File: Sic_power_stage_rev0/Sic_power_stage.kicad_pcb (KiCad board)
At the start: 4 copper layers, 242.5 x 94.5 mm, 153 parts, among them J1 20021321-00006C4LF, J2 20021321-00006C4LF, J3 20021321-00006C4LF, J4 20021321-00006C4LF, J5 20021321-00006C4LF, J6 20021321-00006C4LF, J7 20021321-00006C4LF, J8 20021321-00006C4LF, Q1 NTBG014N120M3P, Q10 NTBG014N120M3P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

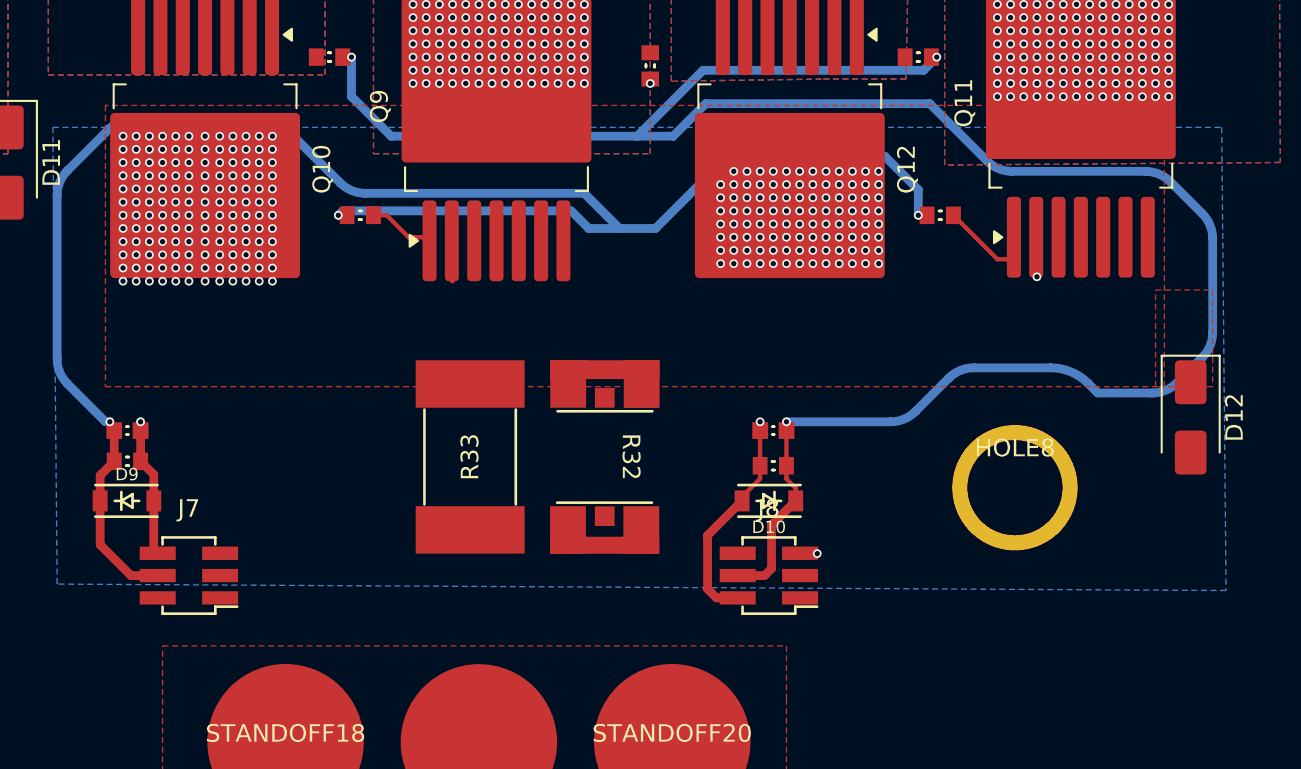
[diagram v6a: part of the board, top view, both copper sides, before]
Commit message: Sic: Define route for SHUNT leg C
Signed-off-by: Ayarde Christian <christianayarde@gmail.com>
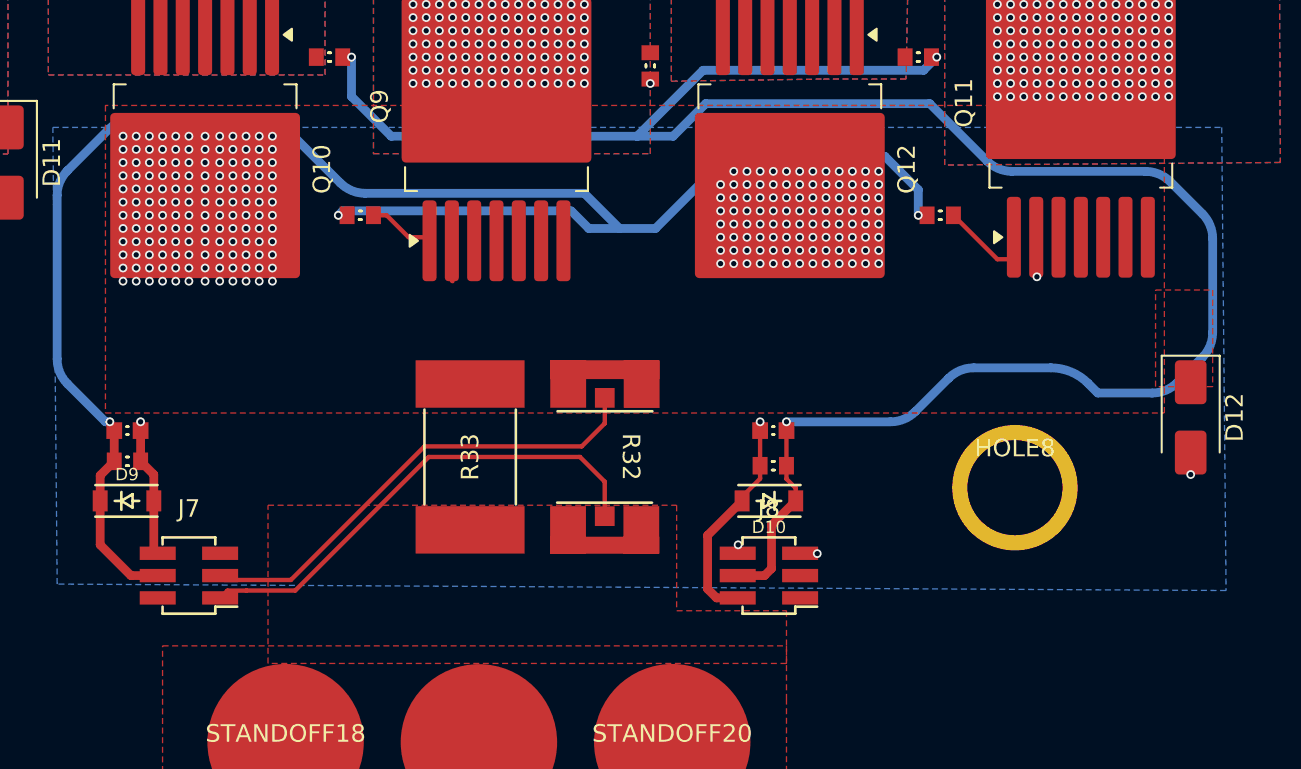
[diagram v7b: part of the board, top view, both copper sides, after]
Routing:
- net /Half Bridge C/D_BOT: track 0.00 -> 32.1 mm, vias 0 -> 2
- net /Half Bridge C/SHUNT-: track 0.00 -> 27.8 mm
- net /Half Bridge C/SHUNT+: track 0.00 -> 27.1 mm
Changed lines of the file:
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@@
 	)
 	(segment
+		(start 55.776 24.356)
+		(end 55.776 24.351)
+		(width 0.25)
+		(layer "F.Cu")
+		(net 22)
+	)
+	(segment
+		(start 76.16 18.16)
+		(end 76.16 20.12)
+		(width 0.25)
+		(layer "F.Cu")
+		(net 22)
+	)
+	(segment
+		(start 55.776 24.351)
+		(end 58.549058 24.351)
+		(width 0.25)
+		(layer "F.Cu")
+		(net 22)
+	)
+	(segment
+		(start 66.150058 16.75)
+		(end 74.75 16.75)
+		(width 0.25)
+		(layer "F.Cu")
+		(net 22)
+	)
+	(segment
+		(start 58.549058 24.351)
+		(end 66.150058 16.75)
+		(width 0.25)
+		(layer "F.Cu")
+		(net 22)
+	)
+	(segment
+		(start 54.275 24.77)
+		(end 54.689 24.356)
+		(width 0.25)
+		(layer "F.Cu")
+		(net 22)
+	)
+	(segment
+		(start 74.75 16.75)
+		(end 76.16 18.16)
+		(width 0.25)
+		(layer "F.Cu")
+		(net 22)
+	)
+	(segment
+		(start 54.689 24.356)
+		(end 55.776 24.356)
+		(width 0.25)
+		(layer "F.Cu")
+		(net 22)
+	)
+	(segment
+		(start 65.901116 16.149)
+		(end 58.300116 23.75)
+		(width 0.25)
+		(layer "F.Cu")
+		(net 23)
+	)
+	(segment
+		(start 76.1615 14.8385)
+		(end 74.851 16.149)
+		(width 0.25)
+		(layer "F.Cu")
+		(net 23)
+	)
+	(segment
+		(start 76.1615 13.389)
+		(end 76.1615 14.8385)
+		(width 0.25)
+		(layer "F.Cu")
+		(net 23)
+	)
+	(segment
+		(start 58.300116 23.75)
+		(end 54.525 23.75)
+		(width 0.25)
+		(layer "F.Cu")
+		(net 23)
+	)
+	(segment
+		(start 54.525 23.75)
+		(end 54.275 23.5)
+		(width 0.25)
+		(layer "F.Cu")
+		(net 23)
+	)
+	(segment
+		(start 74.851 16.149)
+		(end 65.901116 16.149)
+		(width 0.25)
+		(layer "F.Cu")
+		(net 23)
+	)
+	(segment
 		(start 78.75 -4.75)
 		(end 78.75 -4.5)
@@
 	)
 	(segment
+		(start 83.725 21.775)
+		(end 83.75 21.75)
+		(width 0.25)
+		(layer "F.Cu")
+		(net 26)
+	)
+	(segment
+		(start 83.725 22.23)
+		(end 83.725 21.775)
+		(width 0.25)
+		(layer "F.Cu")
+		(net 26)
+	)
+	(segment
+		(start 109.5 16.5)
+		(end 109.5 17.75)
+		(width 0.25)
+		(layer "F.Cu")
+		(net 26)
+	)
+	(via
+		(at 83.75 21.75)
+		(size 0.5)
+		(drill 0.3)
+		(layers "F.Cu" "B.Cu")
+		(net 26)
+	)
+	(via
+		(at 109.5 17.75)
+		(size 0.5)
+		(drill 0.3)
+		(layers "F.Cu" "B.Cu")
+		(net 26)
+	)
+	(segment
+		(start 83.75 21.75)
+		(end 87.196 25.196)
+		(width 0.5)
+		(layer "In2.Cu")
+		(net 26)
+	)
+	(segment
+		(start 87.196 25.196)
+		(end 102.273575 25.196)
+		(width 0.5)
+		(layer "In2.Cu")
+		(net 26)
+	)
+	(segment
+		(start 102.273575 25.196)
+		(end 109.5 17.969575)
+		(width 0.5)
+		(layer "In2.Cu")
+		(net 26)
+	)
+	(segment
+		(start 109.5 17.969575)
+		(end 109.5 17.75)
+		(width 0.25)
+		(layer "In2.Cu")
+		(net 26)
+	)
+	(segment
 		(start -83.5 4.25)
 		(end -82.06 4.25)
@@
 	)
 	(zone
+		(net 31)
+		(net_name "/Half Bridge C/PHASE")
+		(layer "F.Cu")
+		(hatch edge 0.5)
+		(priority 29)
+		(connect_pads yes
+			(clearance 0)
+		)
+		(min_thickness 0.25)
+		(filled_areas_thickness no)
+		(fill yes
+			(thermal_gap 0.5)
+			(thermal_bridge_width 0.5)
+			(smoothing fillet)
+		)
+		(polygon
+			(pts
+				(xy 57 19.5) (xy 80.25 19.5) (xy 80.25 25.5) (xy 86.5 25.5) (xy 86.5 28.5) (xy 57 28.5)
+			)
+		)
+	)
+	(zone
 		(net 67)
 		(net_name "/Half Bridge C/node_a")
@@
 		(polygon
 			(pts
-				(xy 47.75 12.75) (xy 108 12.75) (xy 108 -3.25) (xy 47.75 -3.25)
+				(xy 47.75 14.25) (xy 108 14.25) (xy 108 -3.25) (xy 47.75 -3.25)
 			)
 		)

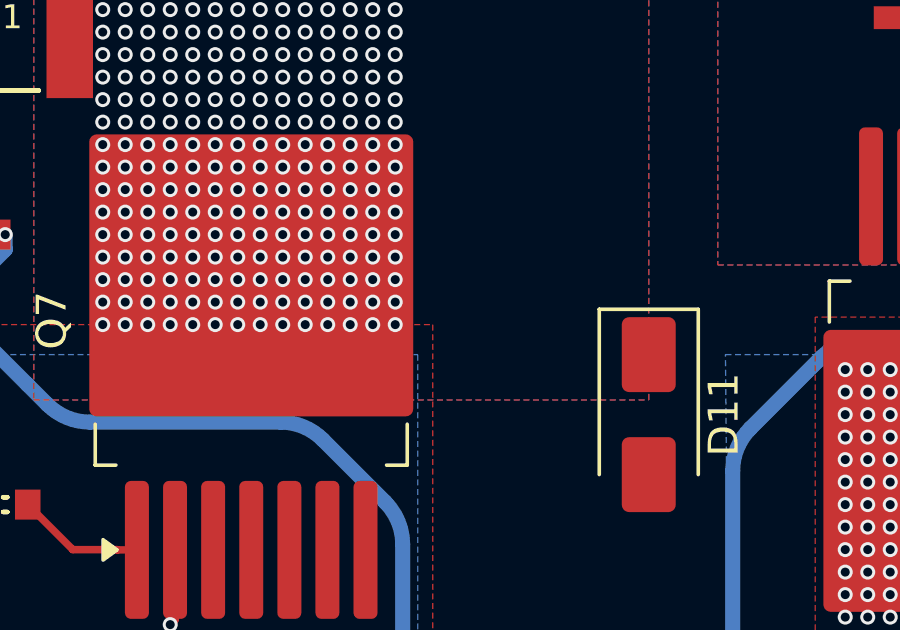
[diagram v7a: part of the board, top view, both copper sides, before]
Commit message: Sic: Increase copper area for thermal dissipation
Signed-off-by: Ayarde Christian <christianayarde@gmail.com>
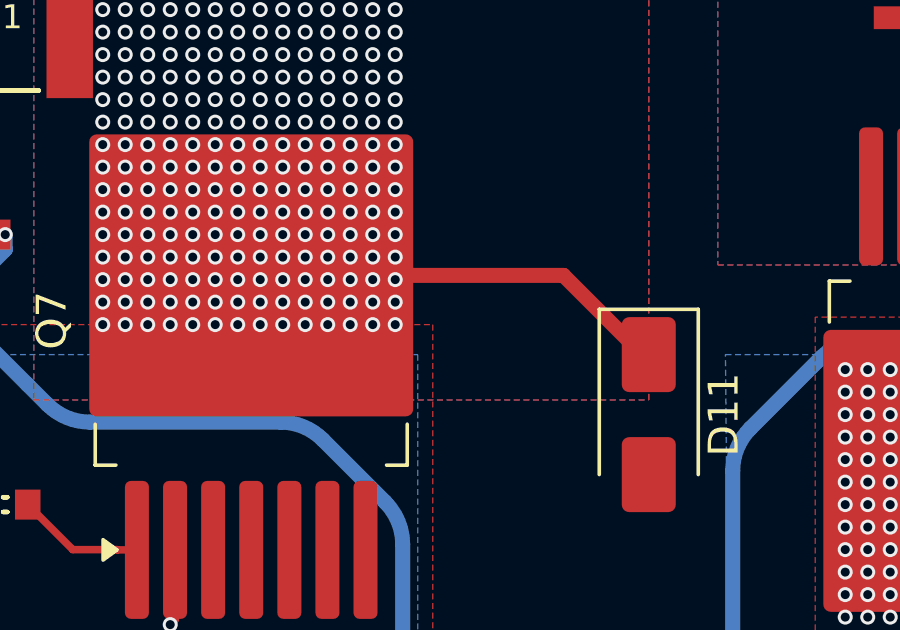
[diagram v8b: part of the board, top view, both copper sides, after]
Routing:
- net VBUS: track 75.3 -> 89.6 mm
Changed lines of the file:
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@@
 	)
 	(segment
+		(start 39.359353 -4.640647)
+		(end 28.95 -4.640647)
+		(width 0.5)
+		(layer "F.Cu")
+		(net 10)
+	)
+	(segment
 		(start -105.999 -4.249)
 		(end -104.251 -2.501)
@@
 	)
 	(segment
+		(start 42.201157 -2)
+		(end 42 -2)
+		(width 0.5)
+		(layer "F.Cu")
+		(net 10)
+	)
+	(segment
 		(start -31.849 -2.501)
 		(end -31.5 -2.501)
@@
 	)
 	(segment
+		(start 42 -2)
+		(end 39.359353 -4.640647)
+		(width 0.5)
+		(layer "F.Cu")
+		(net 10)
+	)
+	(segment
 		(start -86.5 -32.75)
 		(end -102.5 -32.75)
@@
 		(polygon
 			(pts
-				(xy -100 -2.25) (xy -89.75 -2.25) (xy -89.75 7.5) (xy -100 7.5)
+				(xy -104.75 -2.25) (xy -39.5 -2.25) (xy -39.5 23.5) (xy -104.75 23.5)
 			)
 		)
@@
 		(polygon
 			(pts
-				(xy 48.5 -1.75) (xy 57.5 -1.75) (xy 57.5 7) (xy 48.5 7)
+				(xy 45 -2) (xy 111.5 -2) (xy 111.5 24.25) (xy 45 24.25)
 			)
 		)
@@
 		(polygon
 			(pts
-				(xy -25.5 -1.25) (xy -16 -1.25) (xy -16 7.5) (xy -25.5 7.5)
+				(xy -29 -2) (xy 34.5 -2) (xy 34.5 23.75) (xy -29 23.75)
 			)
 		)
